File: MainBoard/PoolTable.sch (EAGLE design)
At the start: 26 parts, among them IC1 LM317MBSTT3, IC2 LM317MBSTT3, IC3 LM317MBSTT3, IC4 USB2517-JZX

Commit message: Added four temp sensors
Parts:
- added R10, R11, R12, R13, R14, R15, R16, R17, R18, R7, R8, R9: 5.6k, SparkFun-Resistors:5.6KOHM-0603-1/10W-1%
- added U1, U2, U3, U4: TMP102, SparkFun-Sensors:TMP102
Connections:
- new net N$10: R13.1, U4.SDA
- new net N$11: R14.1, U4.ADD0, U4.SCL
- new net N$12: R15.1, U4.ALERT
- new net N$13: R16.1, U2.SDA
- new net N$14: R17.1, U2.SCL
- new net N$15: R18.1, U2.ALERT
- new net N$4: R7.1, U1.SDA
- new net N$5: R8.1, U1.SCL
- new net N$6: R9.1, U1.ALERT
- new net N$7: R10.1, U3.ADD0, U3.SDA
- new net N$8: R11.1, U3.SCL
- new net N$9: R12.1, U3.ALERT
- net 3.3V: now also R10.2, R11.2, R12.2, R13.2, R14.2, R15.2, R16.2, R17.2, R18.2, R7.2, R8.2, R9.2, U1.VCC, U2.ADD0, U2.VCC, U3.VCC, U4.VCC
- net GND: now also U1.ADD0, U1.GND, U2.GND, U3.GND, U4.GND
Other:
- note added: "I2C Address: 1001000"
- note added: "I2C Address: 1001001"
- note added: "I2C Address: 1001010"
- note added: "I2C Address: 1001011"

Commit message: Started work on USB Hub/Ethernet
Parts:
- removed R16, R17: 5.6k, SparkFun-Resistors:5.6KOHM-0603-1/10W-1%
- added C10: 1.0uF, SparkFun-Capacitors:1.0UF-0402-16V-10%
- added D7, D8: GREEN, SparkFun-LED:LED-GREEN0603
- added IC5: MIC2026-1YM, micrel:MIC2026-1YM
- added J1, J2: USB_A_SMT_FEMALE, SparkFun-Connectors:USB_A_SMT_FEMALE
- added U$1, U$2, U$3: PWM_MODULE, Modules:PWM_MODULE
- added U$4, U$5: 47uF/6.3V, SparkFun-Capacitors:47UF
- added U5: LAN9512-JZX, External:LAN9512-JZX
- R10, R11, R7, R8: value 5.6k -> 4.7k; device SparkFun-Resistors:5.6KOHM-0603-1/10W-1% -> SparkFun-Resistors:4.7KOHM-0603-1/10W-1%
- R13, R14: value 5.6k -> 150; device SparkFun-Resistors:5.6KOHM-0603-1/10W-1% -> SparkFun-Resistors:150OHM-0603-1/10W-1%
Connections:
- removed net N$13: R16.1, U2.SDA
- removed net N$14: R17.1, U2.SCL
- new net CPU1_ETH_PWR2: D8.A, IC5.OUTA, J2.VBUS, U$4.1
- new net CPU1_ETH_PWR3: D7.A, IC5.OUTB, J1.VBUS, U$5.1
- new net CPU1_ETH_VDD18CORE: U5.VDD18CORE, U5.VDD18CORE_2
- new net CPU1_ETH_VDD3A: U5.VDD33A_1, U5.VDD33A_2, U5.VDD33A_3, U5.VDD33A_4, U5.VDD33A_5, U5.VDD33A_6, U5.VDD33A_7
- new net N$16: D8.C, R13.2
- new net N$17: D7.C, R14.2
- new net PWM1_0: U$1.PWM0
- new net PWM1_1: U$1.PWM1
- new net PWM1_10: U$1.PWM10
- new net PWM1_11: U$1.PWM11
- new net PWM1_12: U$1.PWM12
- new net PWM1_13: U$1.PWM13
- new net PWM1_14: U$1.PWM14
- new net PWM1_15: U$1.PWM15
- new net PWM1_2: U$1.PWM2
- new net PWM1_3: U$1.PWM3
- new net PWM1_4: U$1.PWM4
- new net PWM1_5: U$1.PWM5
- new net PWM1_6: U$1.PWM6
- new net PWM1_7: U$1.PWM7
- new net PWM1_8: U$1.PWM8
- new net PWM1_9: U$1.PWM9
- new net PWM2_0: U$3.PWM0
- new net PWM2_1: U$3.PWM1
- new net PWM2_10: U$3.PWM10
- new net PWM2_11: U$3.PWM11
- new net PWM2_12: U$3.PWM12
- new net PWM2_13: U$3.PWM13
- new net PWM2_14: U$3.PWM14
- new net PWM2_15: U$3.PWM15
- new net PWM2_2: U$3.PWM2
- new net PWM2_3: U$3.PWM3
- new net PWM2_4: U$3.PWM4
- new net PWM2_5: U$3.PWM5
- new net PWM2_6: U$3.PWM6
- new net PWM2_7: U$3.PWM7
- new net PWM2_8: U$3.PWM8
- new net PWM2_9: U$3.PWM9
- new net PWM3_0: U$2.PWM0
- new net PWM3_1: U$2.PWM1
- new net PWM3_10: U$2.PWM10
- new net PWM3_11: U$2.PWM11
- new net PWM3_12: U$2.PWM12
- new net PWM3_13: U$2.PWM13
- new net PWM3_14: U$2.PWM14
- new net PWM3_15: U$2.PWM15
- new net PWM3_2: U$2.PWM2
- new net PWM3_3: U$2.PWM3
- new net PWM3_4: U$2.PWM4
- new net PWM3_5: U$2.PWM5
- new net PWM3_6: U$2.PWM6
- new net PWM3_7: U$2.PWM7
- new net PWM3_8: U$2.PWM8
- new net PWM3_9: U$2.PWM9
- net 3.3V: now also U5.TEST3, U5.VDD33IO_1, U5.VDD33IO_2, U5.VDD33IO_3, U5.VDD33IO_4, U5.VDD33IO_5; no longer R10.2, R11.2, R13.2, R14.2, R16.2, R17.2, R7.2, R8.2
- net 5V: now also C10.2, IC5.IN, R10.2, R11.2, R7.2, R8.2, U$1.5V, U$2.5V, U$3.5V
- net CPU1_SCL0: now also R7.1, U$1.SCL, U$2.SCL, U$3.SCL, U1.SCL, U2.SCL, U3.SCL, U4.ADD0, U4.SCL
- net CPU1_SCL1: now also R10.1
- net CPU1_SDA0: now also R8.1, U$1.SDA, U$2.SDA, U$3.SDA, U1.SDA, U2.SDA, U3.ADD0, U3.SDA, U4.SDA
- net CPU1_SDA1: now also R11.1
- net GND: now also C10.1, IC5.GND, J1.GND, J1.SHIELD, J2.GND, J2.SHIELD, R13.1, R14.1, U$1.GND, U$2.GND, U$3.GND, U$4.2, U$5.2, U5.EPAD, U5.TEST2
- net N$10: now also IC5.ENA, IC5.FLGA, U5.PRTXTL2; no longer R13.1, U4.SDA
- net N$11: now also IC5.ENB, IC5.FLGB, U5.PRTCTL3; no longer R14.1, U4.ADD0, U4.SCL
- net N$4: now also J2.D+, U5.USBDP2; no longer R7.1, U1.SDA
- net N$5: now also J2.D-, U5.USBDM2; no longer R8.1, U1.SCL
- net N$7: now also J1.D+, U5.USBDP3; no longer R10.1, U3.ADD0, U3.SDA
- net N$8: now also J1.D-, U5.USBDM3; no longer R11.1, U3.SCL

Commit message: Implemented boot enable and finished USB
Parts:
- added C11, C14, C15: 0.1uF, SparkFun-Capacitors:0.1UF-0402-16V-10%
- added D9: GREEN, SparkFun-LED:LED-GREEN0603
- added IC7: AP2331W-7, SamacSys_Parts:AP2331W-7
- added J3: (no value), SparkFun-Connectors:USB_MICRO-B_SMT
- added JP1: (no value), adafruit:PINHD-1X3
- added Q1, Q2, Q3: DMG1012T-7, SamacSys_Parts:DMG1012T-7
- added R16, R17, R19: 47k, SparkFun-Resistors:47KOHM-0603-1/10W-1%
- added R20: 150, SparkFun-Resistors:150OHM-0603-1/10W-1%
- added R21: 100K, SparkFun-Resistors:100KOHM-0402-1/16W-1%
- added U6: FSUSB42UMX, FSUSB42UMX:FSUSB42UMX
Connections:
- new net CPU1_EMMC_DISABLE_N: CPU1.2/EMMC_DISABLE_N, Q2.D
- new net CPU1_EMMC_EN_N_1V8: CPU1.90/GPIO47_1V8, Q3.G, R21.2
- new net CPU1_ETH_USBDM: U5.USBDM0, U6.HSD1-
- new net CPU1_ETH_USBDP: U5.USBDP0, U6.HSD1+
- new net CPU1_VBUSB: J3.VBUS, JP1.1, Q1.G, R16.2
- new net H5V: C15.1, IC7.OUT
- new net N$13: CPU1.165/USB_DP**, U6.D+
- new net N$14: CPU1.167/USB_DM**, U6.D-
- new net N$18: J3.D+, U6.HSD2+
- new net N$19: Q1.S, R17.1, U6.SEL
- new net N$20: J3.D-, U6.HSD2-
- new net N$21: JP1.2, Q2.G, R19.2
- new net N$22: D9.C, Q2.S, Q3.D
- new net N$23: D9.A, R20.1
- net 1.8V: now also R21.1
- net 3.3V: now also C11.2, R17.2, R20.2, U6.VCC
- net 5V: now also C14.2, IC7.IN
- net GND: now also C11.1, C14.1, C15.2, IC7.GND, J3.GND, J3.SHIELD, JP1.3, Q1.D, Q3.S, R16.1, R19.1, U6.GND
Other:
- note added: "1-2 USB Boot Enabled 2-3 USB Boot Disabled"
- note added: "USB Boot Enable"

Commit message: Cleaned up Schematic
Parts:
- removed IC4: USB2517-JZX, SamacSys_Parts:USB2517-JZX
- added C12, C13: 4.7uF, SparkFun-Capacitors:4.7UF-0603-6.3V-(10%)
- added J4: SD_CARD_SOCKET, SparkFun-Connectors:SD_CARD_SOCKET
- added R22, R23, R24, R25: 100K, SparkFun-Resistors:100KOHM-0402-1/16W-1%
- added SJ1: (no value), jumper:SJ
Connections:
- net N$13 renamed CPU1_USB_D_P
- net N$14 renamed CPU1_USB_D_N
- removed net N$4: J2.D+, U5.USBDP2
- removed net N$5: J2.D-, U5.USBDM2
- removed net N$7: J1.D+, U5.USBDP3
- removed net N$8: J1.D-, U5.USBDM3
- new net CPU1_ETH_USB_DM2: U5.USBDM2
- new net CPU1_ETH_USB_DM3: U5.USBDM3
- new net CPU1_ETH_USB_DP2: U5.USBDP2
- new net CPU1_ETH_USB_DP3: U5.USBDP3
- new net CPU1_SD_CLK: CPU1.10/NC, J4.CLK
- new net CPU1_SD_CMD: CPU1.12/NC, J4.CMD
- new net CPU1_SD_D0: CPU1.16/NC, J4.DAT0
- new net CPU1_SD_D1: CPU1.18/NC, J4.DAT1
- new net CPU1_SD_D2: CPU1.22/NC, J4.DAT2
- new net CPU1_SD_D3: CPU1.24/NC, J4.CD/DAT3
- new net CPU1_SD_VREF: C13.2, CPU1.4/NC, CPU1.6/NC, SJ1.1
- net 3.3V: now also C12.1, J4.VDD, SJ1.2
- net CPU1_GPIO28: now also R22.1
- net CPU1_GPIO29: now also R23.1
- net CPU1_GPIO44: now also R24.1
- net CPU1_GPIO45: now also R25.1
- net GND: now also C12.2, C13.1, CPU1.14/NC, CPU1.20/NC, CPU1.8/NC, J4.SH@1, J4.SH@2, J4.VSS1, J4.VSS2, R22.2, R23.2, R24.2, R25.2
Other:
- note added: "GPIO 28, 29, 44, 45 DO NOT HAVE PULLS ENABLED AT BOOT SO PROVIDE 100K PULL DOWNS TO AVOID THEM FLOATING"
- note added: "GPIO Pull Downs"
- note added: "HDMI 5V"
- note added: "LAN9512"
- note added: "SD Card"
- note added: "USB Host/Slave Switching"
- note added: "USB Hub/Ethernet"
- note removed: "Network Switch"
- note removed: "USB Hub"
- moved on the sheet: C10, C11, D7, D8, IC5, J1, J2, J3, Q1, R13, R14, R16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

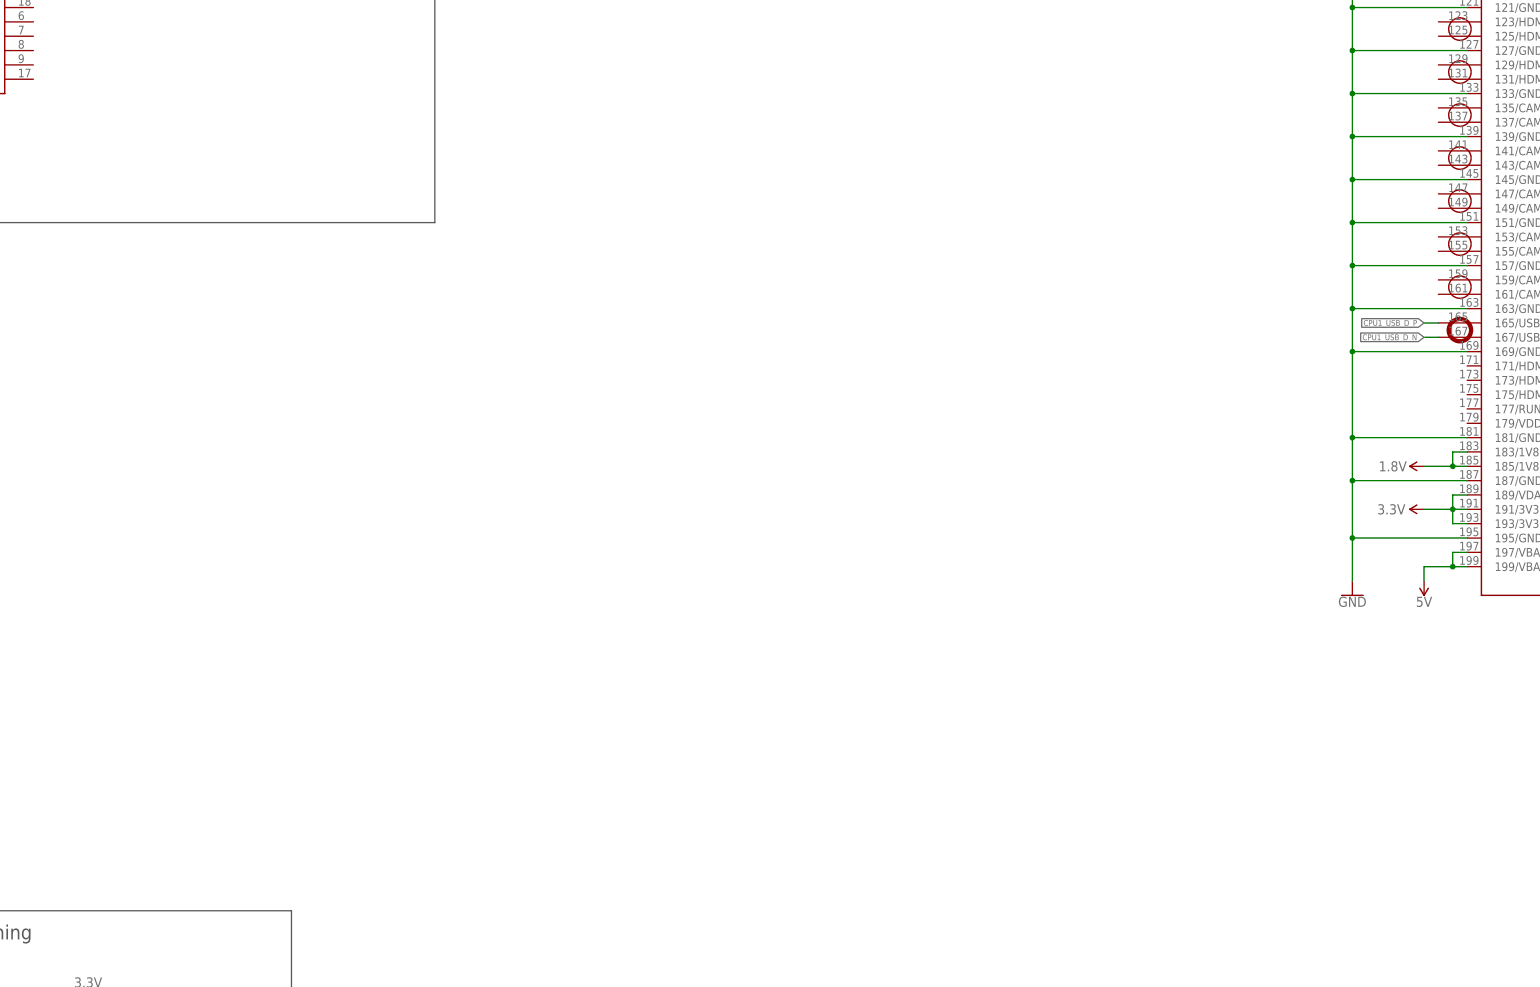
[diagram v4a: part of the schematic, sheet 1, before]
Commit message: Implementing Cameras
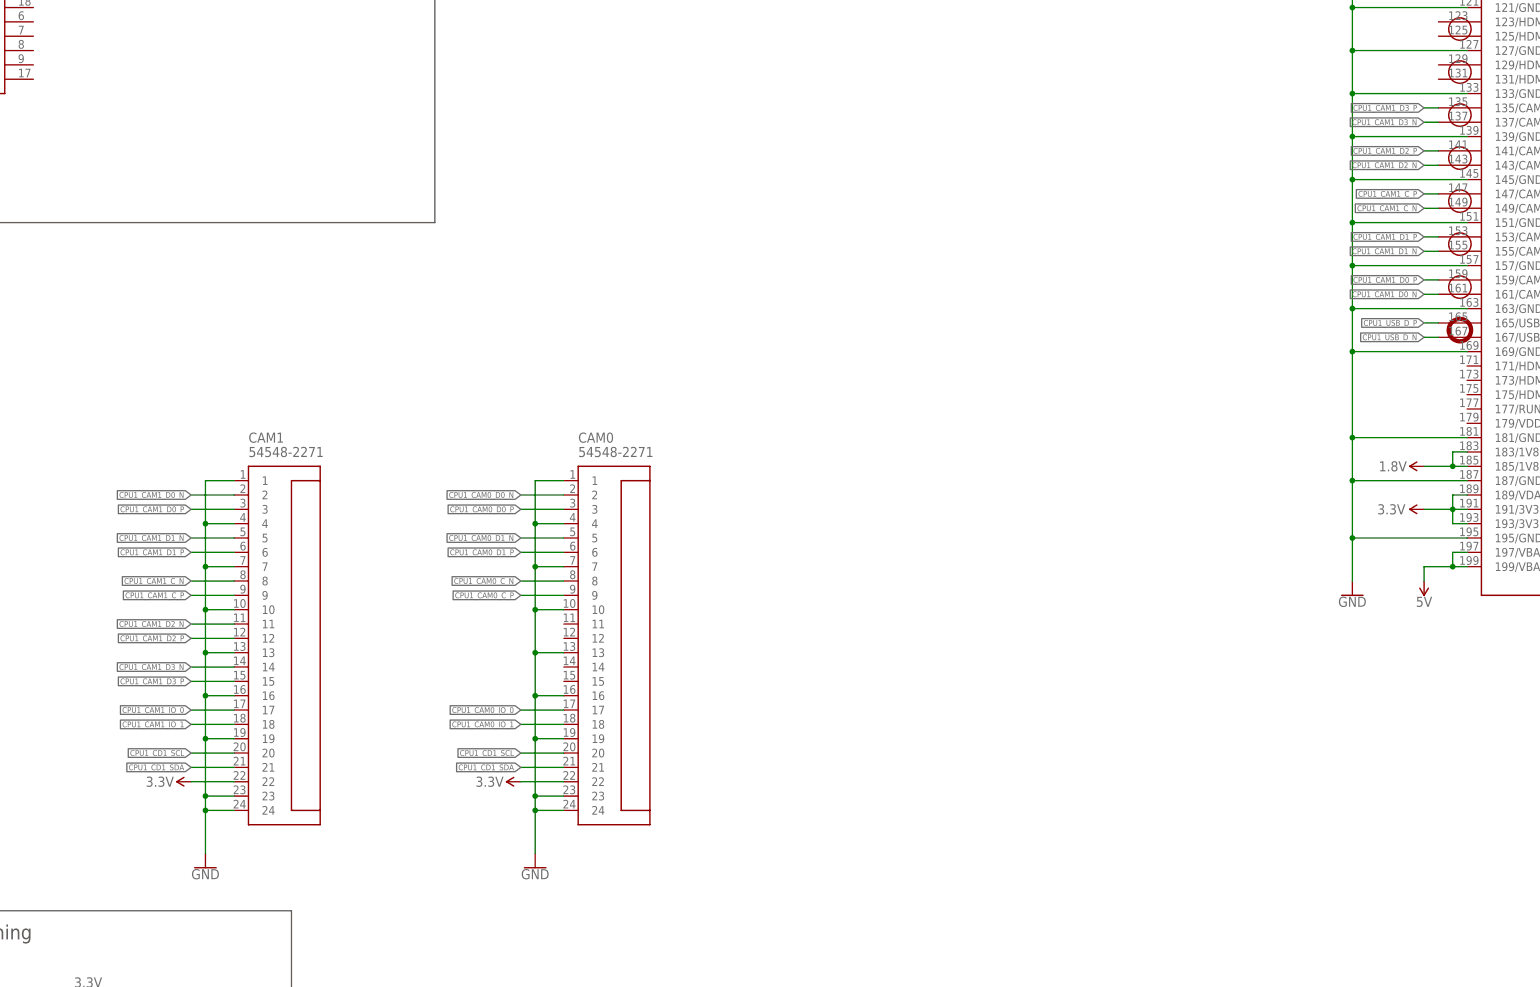
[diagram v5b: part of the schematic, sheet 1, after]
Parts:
- added CAM0, CAM1: 54548-2271, SamacSys_Parts:54548-2271
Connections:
- new net CPU1_CAM0_C_N: CAM0.8
- new net CPU1_CAM0_C_P: CAM0.9
- new net CPU1_CAM0_D0_N: CAM0.2
- new net CPU1_CAM0_D0_P: CAM0.3
- new net CPU1_CAM0_D1_N: CAM0.5
- new net CPU1_CAM0_D1_P: CAM0.6
- new net CPU1_CAM0_IO_0: CAM0.17
- new net CPU1_CAM0_IO_1: CAM0.18
- new net CPU1_CAM1_C_N: CAM1.8, CPU1.149/CAM1_CN*
- new net CPU1_CAM1_C_P: CAM1.9, CPU1.147/CAM1_CP*
- new net CPU1_CAM1_D0_N: CAM1.2, CPU1.161/CAM1_DN0*
- new net CPU1_CAM1_D0_P: CAM1.3, CPU1.159/CAM1_DP0*
- new net CPU1_CAM1_D1_N: CAM1.5, CPU1.155/CAM1_DN1*
- new net CPU1_CAM1_D1_P: CAM1.6, CPU1.153/CAM1_DP1*
- new net CPU1_CAM1_D2_N: CAM1.11, CPU1.143/CAM1_DN2*
- new net CPU1_CAM1_D2_P: CAM1.12, CPU1.141/CAM1_DP2*
- new net CPU1_CAM1_D3_N: CAM1.14, CPU1.137/CAM1_DN3*
- new net CPU1_CAM1_D3_P: CAM1.15, CPU1.135/CAM1_DP3*
- new net CPU1_CAM1_IO_0: CAM1.17
- new net CPU1_CAM1_IO_1: CAM1.18
- new net CPU1_CD1_SCL: CAM0.20, CAM1.20
- new net CPU1_CD1_SDA: CAM0.21, CAM1.21
- net 3.3V: now also CAM0.22, CAM1.22
- net GND: now also CAM0.1, CAM0.10, CAM0.13, CAM0.16, CAM0.19, CAM0.23, CAM0.24, CAM0.4, CAM0.7, CAM1.1, CAM1.10, CAM1.13, CAM1.16, CAM1.19, CAM1.23, CAM1.24, CAM1.4, CAM1.7

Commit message: First HDMI work
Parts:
- added IC4: ESD5384NCTBG, SamacSys_Parts:ESD5384NCTBG
- added Q4: DMG1012T-7, SamacSys_Parts:DMG1012T-7
- added U$6: HDMI-A, connectors:HDMI-A
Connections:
- new net N$4: IC4.SCL, U$6.SCL
- new net N$5: IC4.SDA, U$6.SDA
- new net N$7: IC4.CEC, Q4.S, U$6.CEC
- new net N$8: IC4.HPD, U$6.HOTPLUG
- net GND: now also IC4.GND_1, IC4.GND_2, U$6.CECGND, U$6.CLOCKSHIELD, U$6.DATA0SHIELD, U$6.DATA1SHIELD, U$6.DATA2SHIELD
- net H5V: now also IC4.5V, IC4.RPU, Q4.G, U$6.VCC
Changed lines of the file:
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@@
 <?xml version="1.0" encoding="utf-8"?>
 <!DOCTYPE eagle SYSTEM "eagle.dtd">
-<eagle version="9.3.0">
+<eagle version="9.2.2">
 <drawing>
 <settings>
@@
 <part name="SUPPLY50" library="SparkFun-PowerSymbols" deviceset="3.3V" device=""/>
 <part name="GND22" library="SparkFun-PowerSymbols" deviceset="GND" device=""/>
+<part name="U$6" library="connectors" deviceset="HDMI-A" device=""/>
+<part name="IC4" library="SamacSys_Parts" deviceset="ESD5384NCTBG" device=""/>
+<part name="Q4" library="SamacSys_Parts" deviceset="DMG1012T-7" device=""/>
+<part name="GND23" library="SparkFun-PowerSymbols" deviceset="GND" device=""/>
+<part name="GND24" library="SparkFun-PowerSymbols" deviceset="GND" device=""/>
 </parts>
 <sheets>
@@
 <instance part="GND22" gate="1" x="259.08" y="96.52" smashed="yes">
 <attribute name="VALUE" x="259.08" y="96.266" size="1.778" layer="96" align="top-center"/>
+</instance>
+<instance part="U$6" gate="G$1" x="381" y="48.26" smashed="yes" rot="R180">
+<attribute name="NAME" x="398.78" y="22.86" size="2.54" layer="95" rot="R180"/>
+<attribute name="VALUE" x="398.78" y="81.28" size="2.54" layer="95" rot="R180"/>
+</instance>
+<instance part="IC4" gate="G$1" x="292.1" y="50.8" smashed="yes" rot="R270">
+<attribute name="NAME" x="299.72" y="24.13" size="1.778" layer="95" rot="R270" align="center-left"/>
+<attribute name="VALUE" x="297.18" y="24.13" size="1.778" layer="96" rot="R270" align="center-left"/>
+</instance>
+<instance part="Q4" gate="G$1" x="322.58" y="15.24" smashed="yes">
+<attribute name="NAME" x="334.01" y="19.05" size="1.778" layer="95" align="center-left"/>
+<attribute name="VALUE" x="334.01" y="16.51" size="1.778" layer="96" align="center-left"/>
+</instance>
+<instance part="GND23" gate="1" x="276.86" y="55.88" smashed="yes" rot="R180">
+<attribute name="VALUE" x="276.86" y="56.134" size="1.778" layer="96" rot="R180" align="top-center"/>
+</instance>
+<instance part="GND24" gate="1" x="360.68" y="86.36" smashed="yes" rot="R180">
+<attribute name="VALUE" x="360.68" y="86.614" size="1.778" layer="96" rot="R180" align="top-center"/>
 </instance>
 </instances>
@@
 <pinref part="GND22" gate="1" pin="GND"/>
 </segment>
+<segment>
+<pinref part="IC4" gate="G$1" pin="GND_2"/>
+<wire x1="287.02" y1="20.32" x2="287.02" y2="15.24" width="0.1524" layer="91"/>
+<wire x1="287.02" y1="15.24" x2="276.86" y2="15.24" width="0.1524" layer="91"/>
+<wire x1="276.86" y1="15.24" x2="276.86" y2="50.8" width="0.1524" layer="91"/>
+<pinref part="IC4" gate="G$1" pin="GND_1"/>
+<wire x1="276.86" y1="50.8" x2="281.94" y2="50.8" width="0.1524" layer="91"/>
+<wire x1="276.86" y1="53.34" x2="276.86" y2="50.8" width="0.1524" layer="91"/>
+<junction x="276.86" y="50.8"/>
+<pinref part="GND23" gate="1" pin="GND"/>
+</segment>
+<segment>
+<pinref part="U$6" gate="G$1" pin="DATA2SHIELD"/>
+<wire x1="375.92" y1="63.5" x2="360.68" y2="63.5" width="0.1524" layer="91"/>
+<wire x1="360.68" y1="63.5" x2="360.68" y2="83.82" width="0.1524" layer="91"/>
+<pinref part="U$6" gate="G$1" pin="DATA1SHIELD"/>
+<wire x1="375.92" y1="66.04" x2="360.68" y2="66.04" width="0.1524" layer="91"/>
+<wire x1="360.68" y1="66.04" x2="360.68" y2="63.5" width="0.1524" layer="91"/>
+<junction x="360.68" y="63.5"/>
+<pinref part="U$6" gate="G$1" pin="DATA0SHIELD"/>
+<wire x1="375.92" y1="68.58" x2="360.68" y2="68.58" width="0.1524" layer="91"/>
+<wire x1="360.68" y1="68.58" x2="360.68" y2="66.04" width="0.1524" layer="91"/>
+<junction x="360.68" y="66.04"/>
+<pinref part="U$6" gate="G$1" pin="CLOCKSHIELD"/>
+<wire x1="375.92" y1="71.12" x2="360.68" y2="71.12" width="0.1524" layer="91"/>
+<wire x1="360.68" y1="71.12" x2="360.68" y2="68.58" width="0.1524" layer="91"/>
+<junction x="360.68" y="68.58"/>
+<pinref part="U$6" gate="G$1" pin="CECGND"/>
+<wire x1="375.92" y1="73.66" x2="360.68" y2="73.66" width="0.1524" layer="91"/>
+<wire x1="360.68" y1="73.66" x2="360.68" y2="71.12" width="0.1524" layer="91"/>
+<junction x="360.68" y="71.12"/>
+<pinref part="GND24" gate="1" pin="GND"/>
+</segment>
 </net>
 <net name="CPU1_SDA0" class="0">
@@
 </segment>
 </net>
+<net name="N$4" class="0">
+<segment>
+<pinref part="IC4" gate="G$1" pin="SCL"/>
+<wire x1="287.02" y1="50.8" x2="287.02" y2="55.88" width="0.1524" layer="91"/>
+<pinref part="U$6" gate="G$1" pin="SCL"/>
+<wire x1="287.02" y1="55.88" x2="375.92" y2="55.88" width="0.1524" layer="91"/>
+</segment>
+</net>
+<net name="N$5" class="0">
+<segment>
+<pinref part="IC4" gate="G$1" pin="SDA"/>
+<wire x1="292.1" y1="20.32" x2="304.8" y2="20.32" width="0.1524" layer="91"/>
+<wire x1="304.8" y1="20.32" x2="304.8" y2="53.34" width="0.1524" layer="91"/>
+<pinref part="U$6" gate="G$1" pin="SDA"/>
+<wire x1="304.8" y1="53.34" x2="375.92" y2="53.34" width="0.1524" layer="91"/>
+</segment>
+</net>
+<net name="N$8" class="0">
+<segment>
+<pinref part="IC4" gate="G$1" pin="HPD"/>
+<wire x1="284.48" y1="20.32" x2="284.48" y2="17.78" width="0.1524" layer="91"/>
+<wire x1="284.48" y1="17.78" x2="307.34" y2="17.78" width="0.1524" layer="91"/>
+<wire x1="307.34" y1="17.78" x2="307.34" y2="50.8" width="0.1524" layer="91"/>
+<pinref part="U$6" gate="G$1" pin="HOTPLUG"/>
+<wire x1="307.34" y1="50.8" x2="375.92" y2="50.8" width="0.1524" layer="91"/>
+</segment>
+</net>
+<net name="H5V" class="0">
+<segment>
+<pinref part="U$6" gate="G$1" pin="VCC"/>
+<wire x1="375.92" y1="60.96" x2="373.38" y2="60.96" width="0.1524" layer="91"/>
+<label x="373.38" y="60.96" size="1.016" layer="95" rot="R180" xref="yes"/>
+</segment>
+<segment>
+<pinref part="IC4" gate="G$1" pin="RPU"/>
+<wire x1="289.56" y1="20.32" x2="289.56" y2="15.24" width="0.1524" layer="91"/>
+<wire x1="289.56" y1="15.24" x2="297.18" y2="15.24" width="0.1524" layer="91"/>
+<pinref part="IC4" gate="G$1" pin="5V"/>
+<wire x1="297.18" y1="15.24" x2="297.18" y2="50.8" width="0.1524" layer="91"/>
+<wire x1="297.18" y1="50.8" x2="292.1" y2="50.8" width="0.1524" layer="91"/>
+<pinref part="Q4" gate="G$1" pin="G"/>
+<wire x1="297.18" y1="15.24" x2="314.96" y2="15.24" width="0.1524" layer="91"/>
+<junction x="297.18" y="15.24"/>
+<wire x1="314.96" y1="15.24" x2="322.58" y2="15.24" width="0.1524" layer="91"/>
+<wire x1="314.96" y1="15.24" x2="314.96" y2="20.32" width="0.1524" layer="91"/>
+<junction x="314.96" y="15.24"/>
+<wire x1="314.96" y1="20.32" x2="317.5" y2="20.32" width="0.1524" layer="91"/>
+<label x="317.5" y="20.32" size="1.016" layer="95" xref="yes"/>
+</segment>
+</net>
+<net name="N$7" class="0">
+<segment>
+<pinref part="IC4" gate="G$1" pin="CEC"/>
+<wire x1="289.56" y1="50.8" x2="289.56" y2="58.42" width="0.1524" layer="91"/>
+<pinref part="U$6" gate="G$1" pin="CEC"/>
+<wire x1="289.56" y1="58.42" x2="375.92" y2="58.42" width="0.1524" layer="91"/>
+<wire x1="289.56" y1="58.42" x2="264.16" y2="58.42" width="0.1524" layer="91"/>
+<junction x="289.56" y="58.42"/>
+<wire x1="264.16" y1="58.42" x2="264.16" y2="5.08" width="0.1524" layer="91"/>
+<wire x1="264.16" y1="5.08" x2="330.2" y2="5.08" width="0.1524" layer="91"/>
+<pinref part="Q4" gate="G$1" pin="S"/>
+<wire x1="330.2" y1="5.08" x2="330.2" y2="10.16" width="0.1524" layer="91"/>
+</segment>
+</net>
